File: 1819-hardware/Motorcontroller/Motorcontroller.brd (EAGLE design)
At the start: 38.1 x 38.1 mm, 34 parts, among them U1 GENERIC-SOIC8MSGEQ7N-FILTER, U2 GENERIC-SOIC8MSGEQ7N-FILTER, U3 GENERIC-SOIC8MSGEQ7N-FILTER

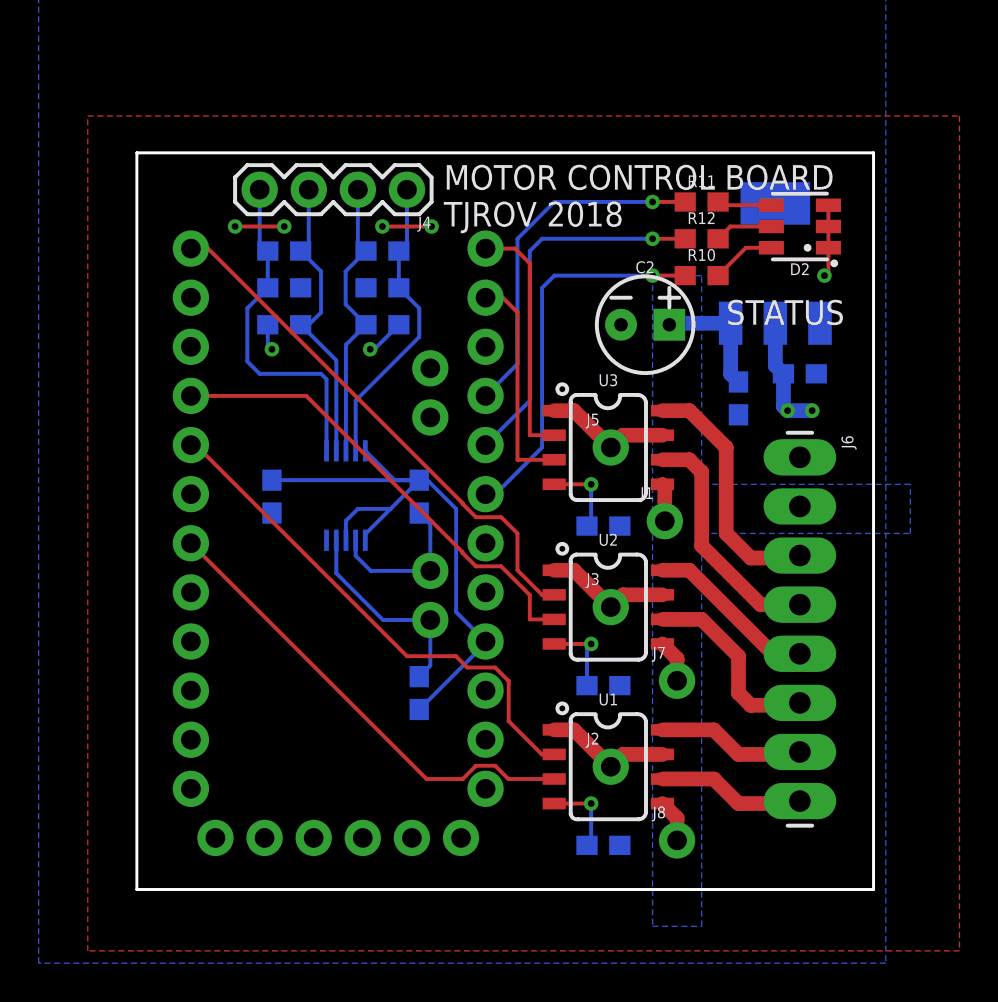
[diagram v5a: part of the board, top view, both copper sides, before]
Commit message: the arduino was upside down
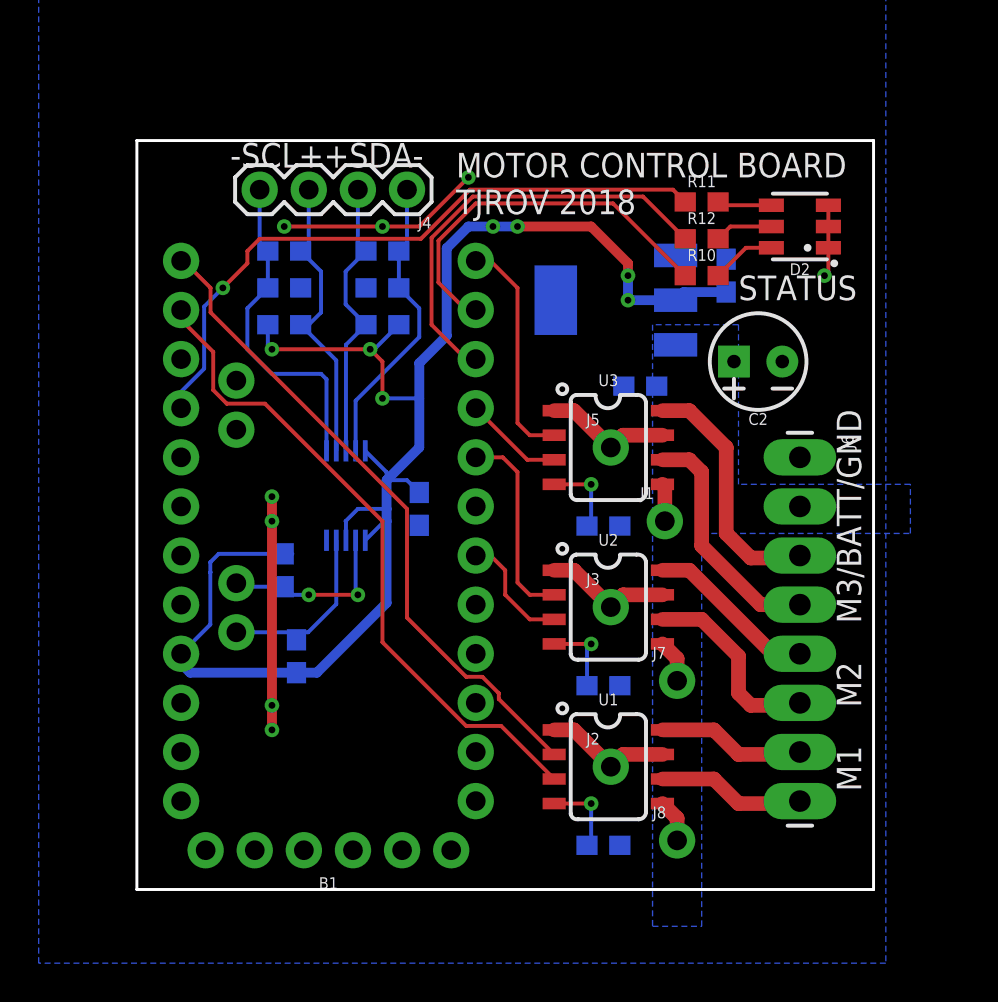
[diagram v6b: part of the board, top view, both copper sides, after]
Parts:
- moved U$1 8.47 mm to (24.8, 30.5), turned to 270 degrees
- moved R4 7.96 mm to (7.62, 16.5)
- moved C3 7.65 mm to (14.6, 19.7)
- moved R1 6.63 mm to (8.26, 12.1)
- moved C1 6.35 mm to (30.5, 31.8), turned to 90 degrees
- moved C2 6.14 mm to (32.1, 27.3), turned to 180 degrees
- moved C6 5.12 mm to (26.0, 26.0), turned to 0 degrees
- moved B1 0.81 mm to (9.91, 17.3), flipped to the top
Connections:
- net GREEN: now also B1.10; no longer B1.17
- net M1IN1: now also B1.14; no longer B1.6
- net M1IN2: now also B1.13; no longer B1.8
- net M2IN1: now also B1.6; no longer B1.9
- net M2IN2: now also B1.8; no longer B1.12
- net M3IN1: now also B1.9; no longer B1.14
- net M3IN2: now also B1.12; no longer B1.13
- net RED: now also B1.11; no longer B1.18
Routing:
- net VCC: track 43.2 -> 82.2 mm, vias 4 -> 7
- net M2IN1: track 24.3 -> 6.17 mm
- net GND: track 28.8 -> 46.3 mm, vias 5 -> 8
- net M2IN2: track 27.3 -> 10.4 mm
- net BLUE: track 18.3 -> 33.8 mm
- net M1IN1: track 24.4 -> 34.5 mm
- net M1IN2: track 26.6 -> 34.1 mm
- net BATT: track 12.8 -> 6.39 mm
- net M3IN1: track 11.5 -> 5.16 mm
- net GREEN: track 19.3 -> 22.4 mm, vias 1 -> 0
- net SDA: track 8.22 -> 9.41 mm, vias 0 -> 2
- net SCL: track 10.7 -> 9.62 mm
- net M3IN2: track 12.8 -> 11.9 mm
- net RED: vias 1 -> 0
- removed copper zone on layer 1, net VCC
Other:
- board size 38.1 x 38.1 mm -> 38.1 x 38.7 mm
- board text added: "-SCL++SDA-"
- board text added: "M1 M2 M3/BATT/GND"

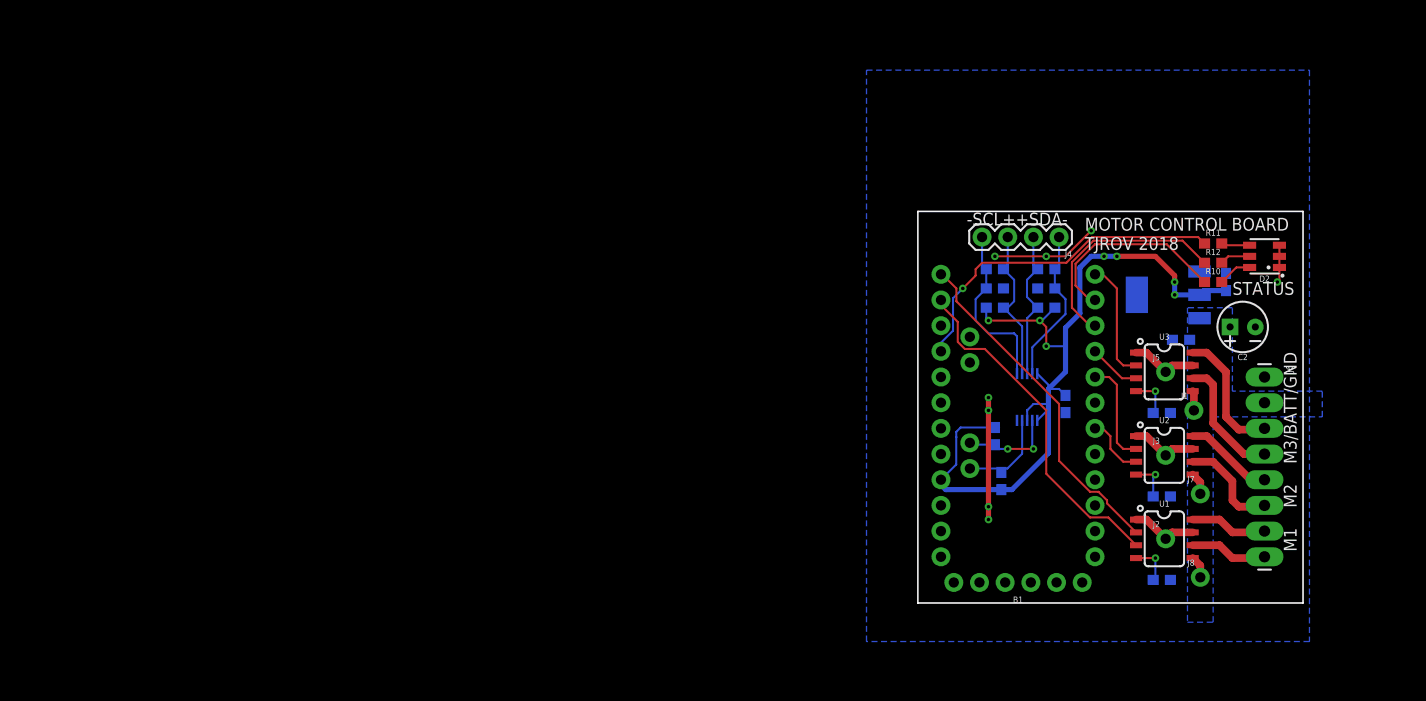
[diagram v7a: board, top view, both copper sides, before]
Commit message: work on motorcontroller pcbs
switching arduino to an i2c device that provides 16 pwm outputs. this will reduce costs and simplify code since we only need one firmware written
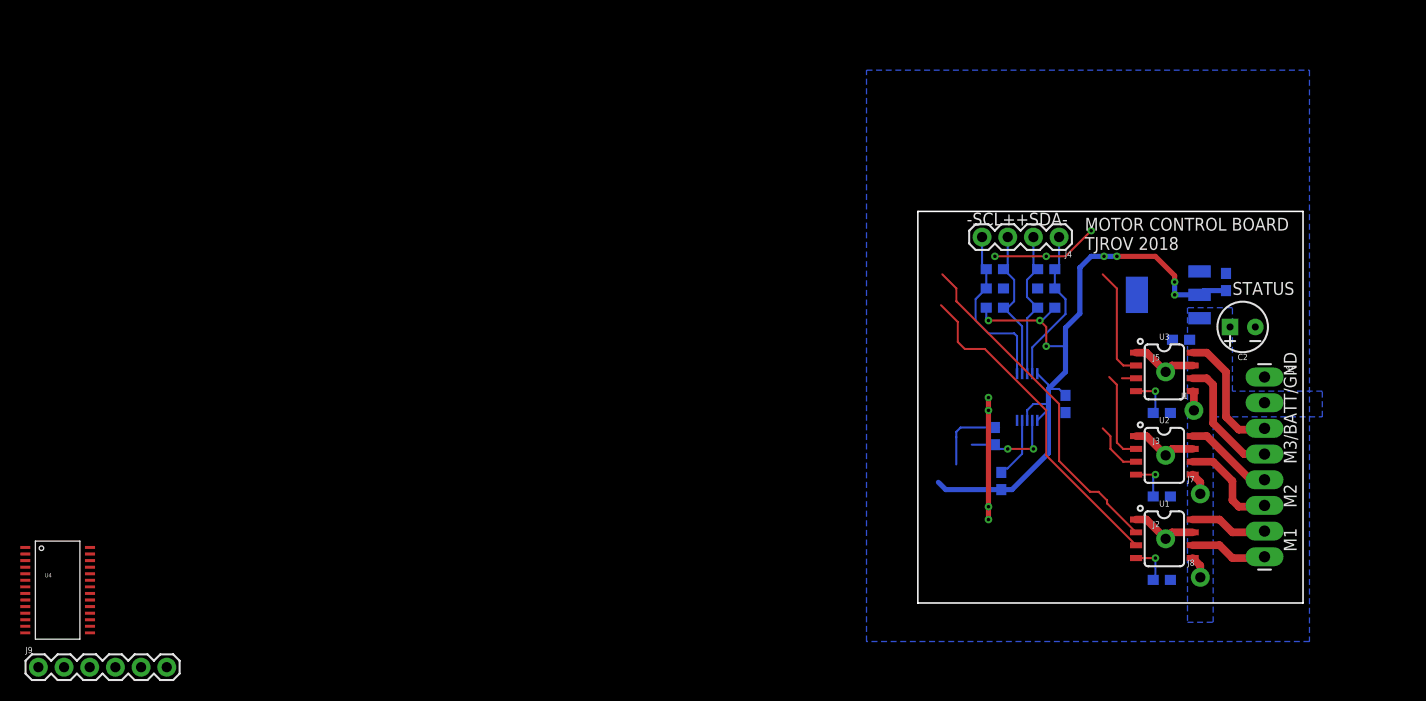
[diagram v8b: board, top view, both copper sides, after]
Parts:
- removed B1: ARDUINO_PRO_MINI, SparkFun-Boards:ARDUINO_PRO_MINI
- removed D2: RGB, SparkFun-LED:PLCC-6-LED
- removed R10, R11, R12: 220, SparkFun-Resistors:0603
- added J9: (no value), SparkFun-Connectors:1X06
- added U4: PCA9685, SparkFun-IC-Special-Function:TSSOP-28_4MM
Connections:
- removed net BLUE: B1.16, R11.1
- removed net GREEN: B1.10, R12.1
- removed net RAW: B1.24
- removed net RED: B1.11, R10.1
- new net ESC1: J9.1
- new net ESC2: J9.2
- new net ESC3: J9.3
- new net ESC4: J9.4
- new net ESC5: J9.5
- new net ESC6: J9.6
- new net N$10: U4.19
- new net N$11: U4.18
- new net N$12: U4.17
- new net N$13: U4.16
- new net N$14: U4.15
- new net N$15: U4.14
- new net N$16: U4.13
- new net N$17: U4.12
- new net N$18: U4.11
- new net N$19: U4.10
- new net N$20: U4.9
- new net N$21: U4.8
- new net N$22: U4.7
- new net N$23: U4.6
- new net N$24: U4.5
- new net N$25: U4.4
- new net N$26: U4.3
- new net N$27: U4.2
- new net N$28: U4.1
- new net N$29: U4.24
- new net N$3: U4.28
- new net N$30: U4.23
- new net N$8: U4.21
- new net N$9: U4.20
- net GND: no longer B1.23, B1.4, D2.CB, D2.CG, D2.CR
- net M1IN1: no longer B1.14
- net M1IN2: no longer B1.13
- net M2IN1: no longer B1.6
- net M2IN2: no longer B1.8
- net M3IN1: no longer B1.9
- net M3IN2: no longer B1.12
- net N$4: now also U4.27; no longer D2.AB, R10.2
- net N$5: now also U4.26; no longer D2.AG, R11.2
- net N$6: now also U4.22; no longer D2.AR, R12.2
- net SCL: no longer B1.A5
- net SDA: no longer B1.A4
- net VCC: no longer B1.21
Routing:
- net BLUE: track 33.8 -> 0.00 mm, vias 1 -> 0
- net GREEN: track 22.4 -> 0.00 mm
- net RED: track 19.8 -> 0.00 mm
- net M3IN1: track 5.16 -> 1.39 mm
- net GND: track 46.3 -> 42.6 mm, vias 8 -> 7
- net SCL: track 9.62 -> 6.12 mm
- net N$4: track 3.35 -> 0.00 mm
- net N$6: track 3.02 -> 0.00 mm
- net N$5: track 2.83 -> 0.00 mm
- net VCC: track 82.2 -> 79.7 mm
- net M1IN1: track 34.5 -> 32.9 mm
- net M2IN2: track 10.4 -> 8.95 mm
- net M3IN2: track 11.9 -> 11.1 mm
- net M2IN1: track 6.17 -> 5.41 mm
